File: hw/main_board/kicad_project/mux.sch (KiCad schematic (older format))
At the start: 14 parts

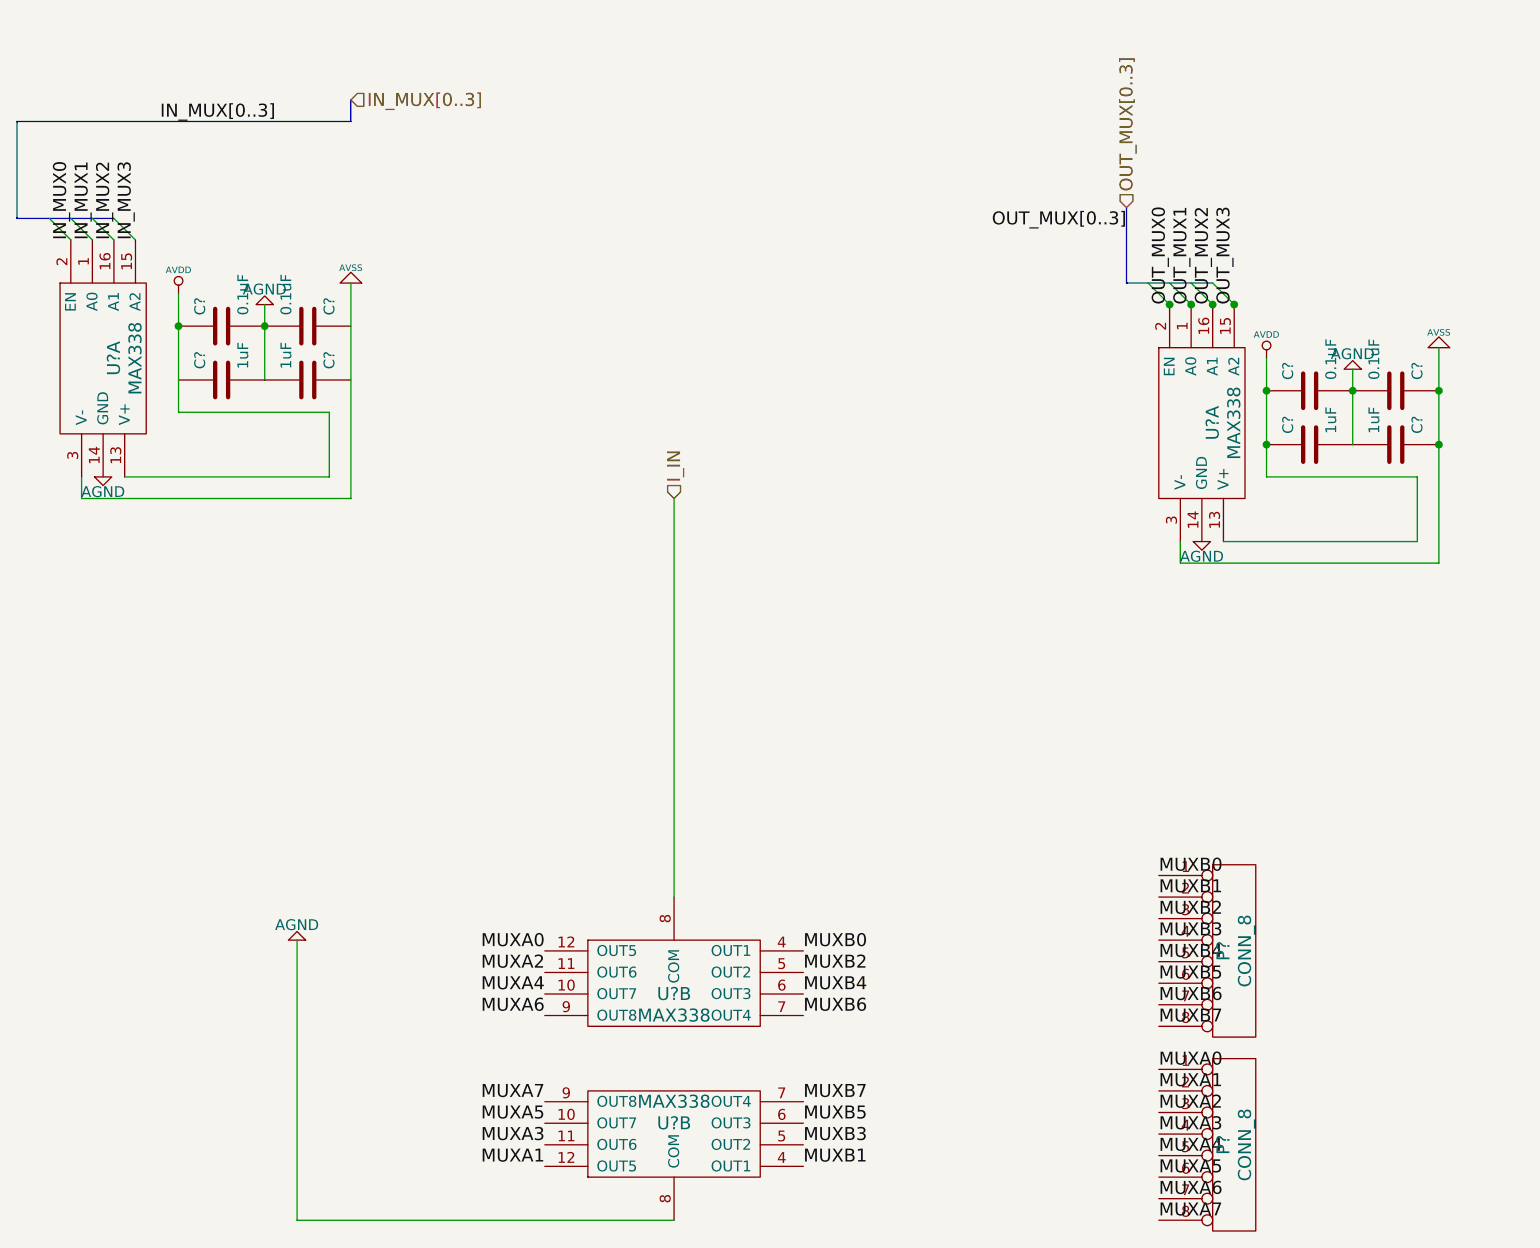
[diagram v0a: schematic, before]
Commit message: started mainboard pcb layout, fixing small things in schematic, TODO: schematic connector symbols and pads
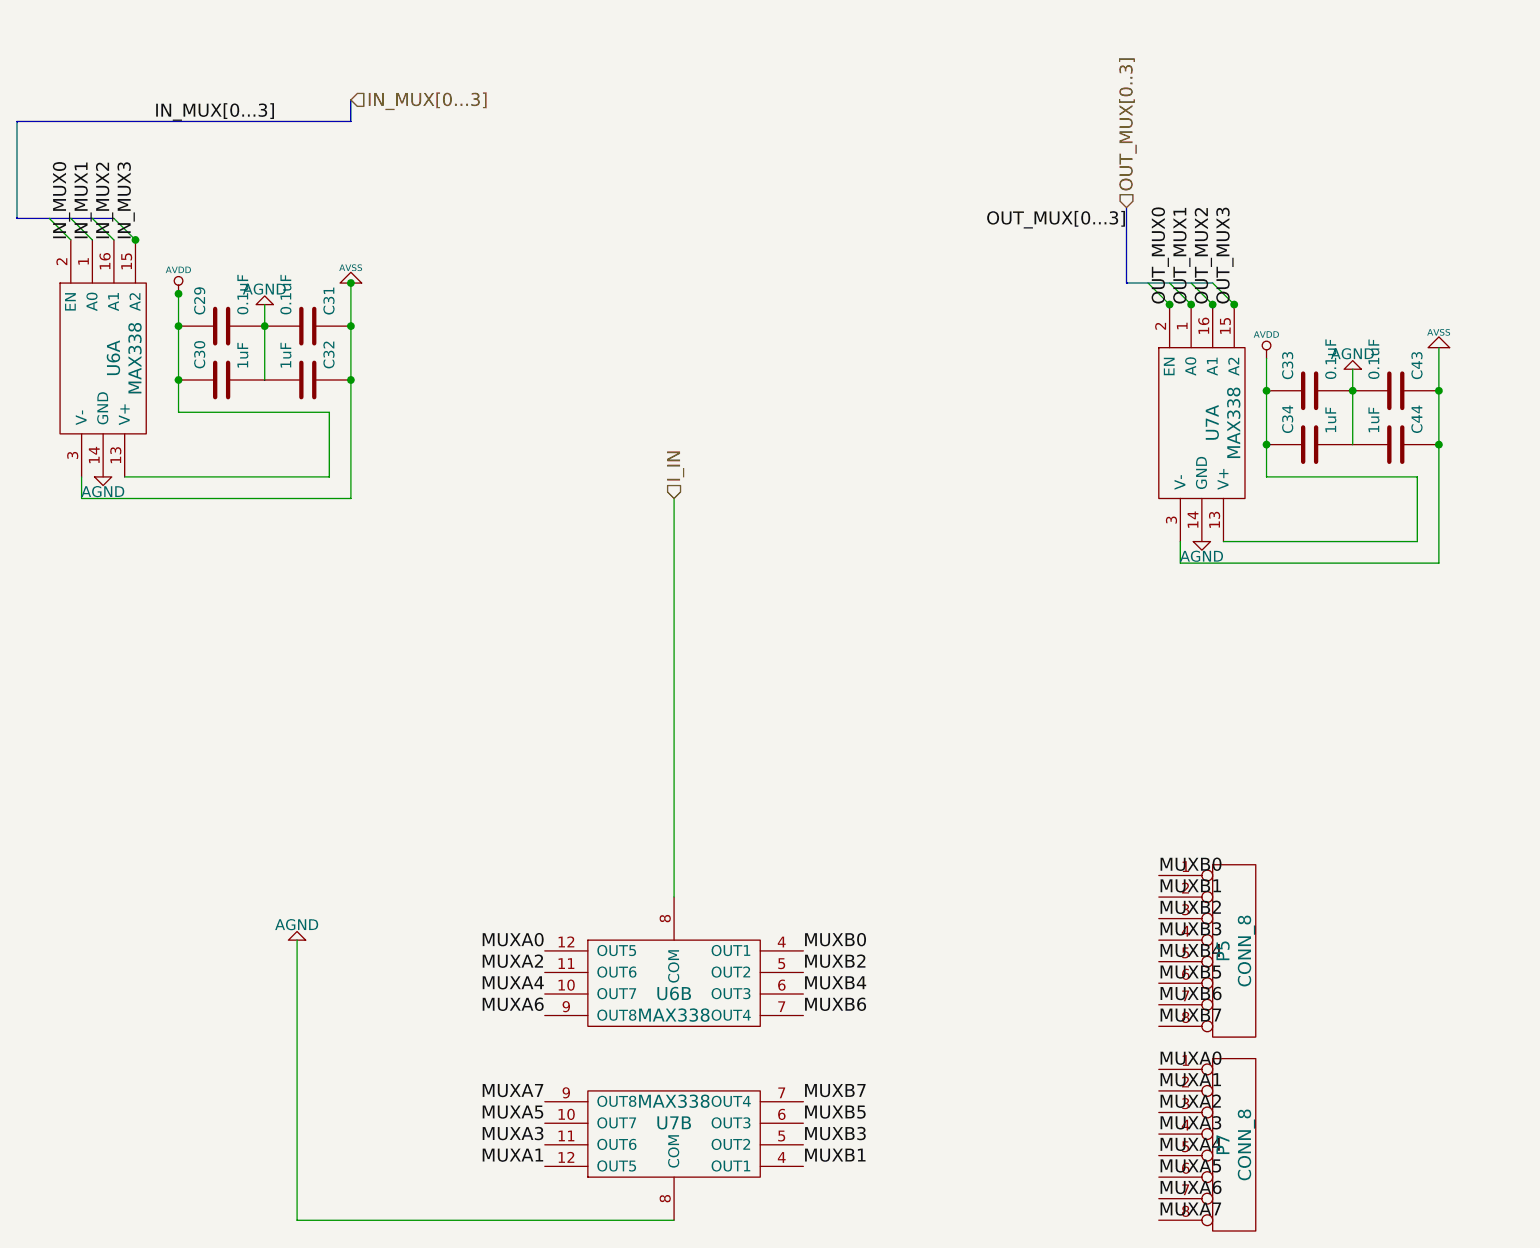
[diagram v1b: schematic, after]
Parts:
- C29, C30, C31, C32, C33, C34, C43, C44: renamed from C?; footprint (none) -> 0603
- U6, U7: renamed from U?; footprint (none) -> QSOP_16
- gave numbers to parts that had none: 2
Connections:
- net AVDD: now also C30.1
- net AVSS: now also C31.1, C32.1
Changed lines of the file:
@@
 encoding utf-8
 Sheet 7 7
-Title ""
-Date ""
-Rev ""
+Title "Output Multiplexer"
+Date "01 Feb 2014"
+Rev "A"
 Comp ""
-Comment1 ""
+Comment1 "Copyright 2014 Andrey Shmakov"
 Comment2 ""
 Comment3 ""
@@
 MUXA0
 $Comp
-L AGND #PWR?
+L AGND #PWR047
 U 1 1 53170BAB
 P 5650 4800
-F 0 "#PWR?" H 5650 4800 40  0001 C CNN
+F 0 "#PWR047" H 5650 4800 40  0001 C CNN
 F 1 "AGND" H 5650 4730 50  0000 C CNN
 F 2 "" H 5650 4800 60  0001 C CNN
@@
 P 7400 5700
 AR Path="/53170BB1" Ref="U?"  Part="2"
-AR Path="/531703E6/53170BB1" Ref="U?"  Part="2"
-F 0 "U?" H 7400 5650 60  0000 C CNN
+AR Path="/531703E6/53170BB1" Ref="U7"  Part="2"
+F 0 "U7" H 7400 5650 60  0000 C CNN
 F 1 "MAX338" H 7400 5550 60  0000 C CNN
-F 2 "" H 7400 5700 60  0001 C CNN
+F 2 "QSOP_16" H 7400 5700 60  0001 C CNN
 F 3 "" H 7400 5700 60  0001 C CNN
 	2    7400 5700
@@
 P 7400 5000
 AR Path="/53170BB7" Ref="U?"  Part="2"
-AR Path="/531703E6/53170BB7" Ref="U?"  Part="2"
-F 0 "U?" H 7400 4950 60  0000 C CNN
+AR Path="/531703E6/53170BB7" Ref="U6"  Part="2"
+F 0 "U6" H 7400 4950 60  0000 C CNN
 F 1 "MAX338" H 7400 4850 60  0000 C CNN
-F 2 "" H 7400 5000 60  0001 C CNN
+F 2 "QSOP_16" H 7400 5000 60  0001 C CNN
 F 3 "" H 7400 5000 60  0001 C CNN
 	2    7400 5000
@@
 	9600 1750 9700 1850
 $Comp
-L AGND #PWR?
+L AGND #PWR048
 U 1 1 53170CB9
 P 9850 2950
-F 0 "#PWR?" H 9850 2950 40  0001 C CNN
+F 0 "#PWR048" H 9850 2950 40  0001 C CNN
 F 1 "AGND" H 9850 2880 50  0000 C CNN
 F 2 "" H 9850 2950 60  0001 C CNN
@@
 $EndComp
 $Comp
-L AVSS #PWR?
+L AVSS #PWR049
 U 1 1 53170CBF
 P 10950 2050
-F 0 "#PWR?" H 10950 2050 30  0001 C CNN
+F 0 "#PWR049" H 10950 2050 30  0001 C CNN
 F 1 "AVSS" H 10950 1980 30  0000 C CNN
 F 2 "" H 10950 2050 60  0001 C CNN
@@
 $EndComp
 $Comp
-L C C?
+L C C43
 U 1 1 53170CC5
 P 10750 2250
-F 0 "C?" H 10800 2350 50  0000 L CNN
+F 0 "C43" H 10800 2350 50  0000 L CNN
 F 1 "0.1uF" H 10800 2150 50  0000 L CNN
-F 2 "" H 10750 2250 60  0001 C CNN
+F 2 "0603" H 10750 2250 60  0001 C CNN
 F 3 "" H 10750 2250 60  0001 C CNN
 	1    10750 2250
@@
 $EndComp
 $Comp
-L C C?
+L C C44
 U 1 1 53170CCB
 P 10750 2500
-F 0 "C?" H 10800 2600 50  0000 L CNN
+F 0 "C44" H 10800 2600 50  0000 L CNN
 F 1 "1uF" H 10800 2400 50  0000 L CNN
-F 2 "" H 10750 2500 60  0001 C CNN
+F 2 "0603" H 10750 2500 60  0001 C CNN
 F 3 "" H 10750 2500 60  0001 C CNN
 	1    10750 2500
@@
 $EndComp
 $Comp
-L AVDD #PWR?
+L AVDD #PWR050
 U 1 1 53170CD1
 P 10150 2100
-F 0 "#PWR?" H 10150 2200 30  0001 C CNN
+F 0 "#PWR050" H 10150 2200 30  0001 C CNN
 F 1 "AVDD" H 10150 2210 30  0000 C CNN
 F 2 "" H 10150 2100 60  0001 C CNN
@@
 $EndComp
 $Comp
-L AGND #PWR?
+L AGND #PWR051
 U 1 1 53170CD7
 P 10550 2150
-F 0 "#PWR?" H 10550 2150 40  0001 C CNN
+F 0 "#PWR051" H 10550 2150 40  0001 C CNN
 F 1 "AGND" H 10550 2080 50  0000 C CNN
 F 2 "" H 10550 2150 60  0001 C CNN
@@
 $EndComp
 $Comp
-L C C?
+L C C33
 U 1 1 53170CDD
 P 10350 2250
-F 0 "C?" H 10400 2350 50  0000 L CNN
+F 0 "C33" H 10400 2350 50  0000 L CNN
 F 1 "0.1uF" H 10400 2150 50  0000 L CNN
-F 2 "" H 10350 2250 60  0001 C CNN
+F 2 "0603" H 10350 2250 60  0001 C CNN
 F 3 "" H 10350 2250 60  0001 C CNN
 	1    10350 2250
@@
 $EndComp
 $Comp
-L C C?
+L C C34
 U 1 1 53170CE3
 P 10350 2500
-F 0 "C?" H 10400 2600 50  0000 L CNN
+F 0 "C34" H 10400 2600 50  0000 L CNN
 F 1 "1uF" H 10400 2400 50  0000 L CNN
-F 2 "" H 10350 2500 60  0001 C CNN
+F 2 "0603" H 10350 2500 60  0001 C CNN
 F 3 "" H 10350 2500 60  0001 C CNN
 	1    10350 2500
@@
 P 9850 2400
 AR Path="/53170CE9" Ref="U?"  Part="1"
-AR Path="/531703E6/53170CE9" Ref="U?"  Part="1"
-F 0 "U?" H 9850 2350 60  0000 C CNN
+AR Path="/531703E6/53170CE9" Ref="U7"  Part="1"
+F 0 "U7" H 9850 2350 60  0000 C CNN
 F 1 "MAX338" H 9850 2250 60  0000 C CNN
-F 2 "" H 9850 2400 60  0001 C CNN
+F 2 "QSOP_16" H 9850 2400 60  0001 C CNN
 F 3 "" H 9850 2400 60  0001 C CNN
 	1    9850 2400
@@
 	4500 1450 4600 1550
 $Comp
-L AGND #PWR?
+L AGND #PWR052
 U 1 1 53171190
 P 4750 2650
-F 0 "#PWR?" H 4750 2650 40  0001 C CNN
+F 0 "#PWR052" H 4750 2650 40  0001 C CNN
 F 1 "AGND" H 4750 2580 50  0000 C CNN
 F 2 "" H 4750 2650 60  0001 C CNN
@@
 $EndComp
 $Comp
-L C C?
+L C C30
 U 1 1 53171196
 P 5300 2200
-F 0 "C?" H 5350 2300 50  0000 L CNN
+F 0 "C30" H 5350 2300 50  0000 L CNN
 F 1 "1uF" H 5350 2100 50  0000 L CNN
-F 2 "" H 5300 2200 60  0001 C CNN
+F 2 "0603" H 5300 2200 60  0001 C CNN
 F 3 "" H 5300 2200 60  0001 C CNN
 	1    5300 2200
@@
 $EndComp
 $Comp
-L C C?
+L C C29
 U 1 1 5317119C
 P 5300 1950
-F 0 "C?" H 5350 2050 50  0000 L CNN
+F 0 "C29" H 5350 2050 50  0000 L CNN
 F 1 "0.1uF" H 5350 1850 50  0000 L CNN
-F 2 "" H 5300 1950 60  0001 C CNN
+F 2 "0603" H 5300 1950 60  0001 C CNN
 F 3 "" H 5300 1950 60  0001 C CNN
 	1    5300 1950
@@
 $EndComp
 $Comp
-L AGND #PWR?
+L AGND #PWR053
 U 1 1 531711A2
 P 5500 1850
-F 0 "#PWR?" H 5500 1850 40  0001 C CNN
+F 0 "#PWR053" H 5500 1850 40  0001 C CNN
 F 1 "AGND" H 5500 1780 50  0000 C CNN
 F 2 "" H 5500 1850 60  0001 C CNN
@@
 $EndComp
 $Comp
-L AVDD #PWR?
+L AVDD #PWR054
 U 1 1 531711A8
 P 5100 1800
-F 0 "#PWR?" H 5100 1900 30  0001 C CNN
+F 0 "#PWR054" H 5100 1900 30  0001 C CNN
 F 1 "AVDD" H 5100 1910 30  0000 C CNN
 F 2 "" H 5100 1800 60  0001 C CNN
@@
 $EndComp
 $Comp
-L C C?
+L C C32
 U 1 1 531711AE
 P 5700 2200
-F 0 "C?" H 5750 2300 50  0000 L CNN
+F 0 "C32" H 5750 2300 50  0000 L CNN
 F 1 "1uF" H 5750 2100 50  0000 L CNN
-F 2 "" H 5700 2200 60  0001 C CNN
+F 2 "0603" H 5700 2200 60  0001 C CNN
 F 3 "" H 5700 2200 60  0001 C CNN
 	1    5700 2200
@@
 $EndComp
 $Comp
-L C C?
+L C C31
 U 1 1 531711B4
 P 5700 1950
-F 0 "C?" H 5750 2050 50  0000 L CNN
+F 0 "C31" H 5750 2050 50  0000 L CNN
 F 1 "0.1uF" H 5750 1850 50  0000 L CNN
-F 2 "" H 5700 1950 60  0001 C CNN
+F 2 "0603" H 5700 1950 60  0001 C CNN
 F 3 "" H 5700 1950 60  0001 C CNN
 	1    5700 1950
@@
 $EndComp
 $Comp
-L AVSS #PWR?
+L AVSS #PWR055
 U 1 1 531711BA
 P 5900 1750
-F 0 "#PWR?" H 5900 1750 30  0001 C CNN
+F 0 "#PWR055" H 5900 1750 30  0001 C CNN
 F 1 "AVSS" H 5900 1680 30  0000 C CNN
 F 2 "" H 5900 1750 60  0001 C CNN
@@
 P 4750 2100
 AR Path="/531711C0" Ref="U?"  Part="1"
-AR Path="/531703E6/531711C0" Ref="U?"  Part="1"
-F 0 "U?" H 4750 2050 60  0000 C CNN
+AR Path="/531703E6/531711C0" Ref="U6"  Part="1"
+F 0 "U6" H 4750 2050 60  0000 C CNN
 F 1 "MAX338" H 4750 1950 60  0000 C CNN
-F 2 "" H 4750 2100 60  0001 C CNN
+F 2 "QSOP_16" H 4750 2100 60  0001 C CNN
 F 3 "" H 4750 2100 60  0001 C CNN
 	1    4750 2100
@@
 	5900 1000 5900 900
 Text HLabel 5900 900  2    60   Input ~ 0
-IN_MUX[0..3]
+IN_MUX[0...3]
 Text Label 5550 1000 2    60   ~ 0
-IN_MUX[0..3]
+IN_MUX[0...3]
 Text HLabel 9500 1400 1    60   Input ~ 0
 OUT_MUX[0..3]
 Text Label 9500 1500 2    60   ~ 0
-OUT_MUX[0..3]
+OUT_MUX[0...3]
 Text Label 9650 5200 0    60   ~ 0
 MUXB7
@@
 MUXA0
 $Comp
-L CONN_8 P?
+L CONN_8 P7
 U 1 1 53171513
 P 10000 5750
-F 0 "P?" V 9950 5750 60  0000 C CNN
+F 0 "P7" V 9950 5750 60  0000 C CNN
 F 1 "CONN_8" V 10050 5750 60  0000 C CNN
 F 2 "" H 10000 5750 60  0001 C CNN
@@
 $EndComp
 $Comp
-L CONN_8 P?
+L CONN_8 P5
 U 1 1 53171519
 P 10000 4850
-F 0 "P?" V 9950 4850 60  0000 C CNN
+F 0 "P5" V 9950 4850 60  0000 C CNN
 F 1 "CONN_8" V 10050 4850 60  0000 C CNN
 F 2 "" H 10000 4850 60  0001 C CNN
@@
 Text HLabel 7400 2750 1    60   Input ~ 0
 I_IN
+Connection ~ 5100 2200
+Connection ~ 5900 2200
+Connection ~ 5900 1950
+Connection ~ 5900 1750
+Connection ~ 5100 1800
+Connection ~ 4900 1550
 $EndSCHEMATC
